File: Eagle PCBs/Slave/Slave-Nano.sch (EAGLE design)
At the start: 15 parts, among them Q1 TIP120

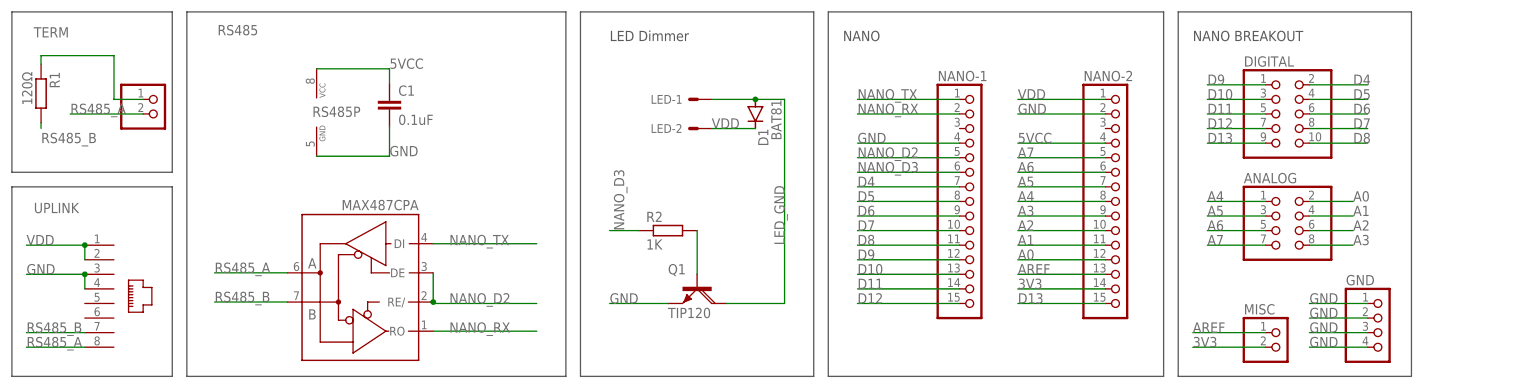
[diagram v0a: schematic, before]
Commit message: Added a 5v bus to all PCBs
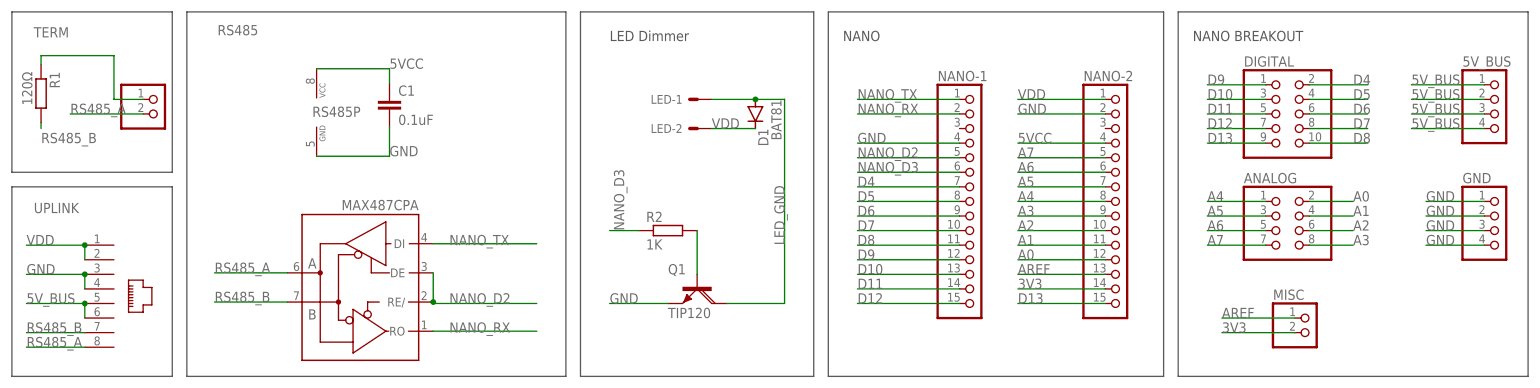
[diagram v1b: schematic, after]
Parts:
- added 5V_BUS: (no value), pinhead:PINHD-1X4
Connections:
- new net 5V_BUS: 5V_BUS.1, 5V_BUS.2, 5V_BUS.3, 5V_BUS.4, UPLINK.5, UPLINK.6
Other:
- moved on the sheet: GND, MISC
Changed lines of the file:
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@@
 <part name="MISC" library="pinhead" library_urn="urn:adsk.eagle:library:325" deviceset="PINHD-1X2" device="" package3d_urn="urn:adsk.eagle:package:22435/2"/>
 <part name="GND" library="pinhead" library_urn="urn:adsk.eagle:library:325" deviceset="PINHD-1X4" device="" package3d_urn="urn:adsk.eagle:package:22407/2"/>
+<part name="5V_BUS" library="pinhead" library_urn="urn:adsk.eagle:library:325" deviceset="PINHD-1X4" device="" package3d_urn="urn:adsk.eagle:package:22407/2"/>
 </parts>
 <sheets>
@@
 <wire x1="144.78" y1="2.54" x2="144.78" y2="66.04" width="0.1524" layer="97"/>
 <text x="147.32" y="60.96" size="1.778" layer="97">NANO</text>
-<wire x1="205.74" y1="66.04" x2="246.38" y2="66.04" width="0.1524" layer="97"/>
-<wire x1="246.38" y1="66.04" x2="246.38" y2="2.54" width="0.1524" layer="97"/>
-<wire x1="246.38" y1="2.54" x2="205.74" y2="2.54" width="0.1524" layer="97"/>
+<wire x1="205.74" y1="66.04" x2="266.7" y2="66.04" width="0.1524" layer="97"/>
+<wire x1="266.7" y1="66.04" x2="266.7" y2="2.54" width="0.1524" layer="97"/>
+<wire x1="266.7" y1="2.54" x2="205.74" y2="2.54" width="0.1524" layer="97"/>
 <wire x1="205.74" y1="2.54" x2="205.74" y2="66.04" width="0.1524" layer="97"/>
 <text x="208.28" y="60.96" size="1.778" layer="97">NANO BREAKOUT</text>
@@
 <attribute name="VALUE" x="217.17" y="20.32" size="1.778" layer="96"/>
 </instance>
-<instance part="MISC" gate="G$1" x="223.52" y="7.62" smashed="yes">
-<attribute name="NAME" x="217.17" y="13.335" size="1.778" layer="95"/>
-<attribute name="VALUE" x="217.17" y="2.54" size="1.778" layer="96"/>
-</instance>
-<instance part="GND" gate="A" x="241.3" y="10.16" smashed="yes">
-<attribute name="NAME" x="234.95" y="18.415" size="1.778" layer="95"/>
-<attribute name="VALUE" x="234.95" y="2.54" size="1.778" layer="96"/>
+<instance part="MISC" gate="G$1" x="228.6" y="10.16" smashed="yes">
+<attribute name="NAME" x="222.25" y="15.875" size="1.778" layer="95"/>
+<attribute name="VALUE" x="222.25" y="5.08" size="1.778" layer="96"/>
+</instance>
+<instance part="GND" gate="A" x="261.62" y="27.94" smashed="yes">
+<attribute name="NAME" x="255.27" y="36.195" size="1.778" layer="95"/>
+<attribute name="VALUE" x="255.27" y="20.32" size="1.778" layer="96"/>
+</instance>
+<instance part="5V_BUS" gate="A" x="261.62" y="48.26" smashed="yes">
+<attribute name="NAME" x="255.27" y="56.515" size="1.778" layer="95"/>
+<attribute name="VALUE" x="255.27" y="40.64" size="1.778" layer="96"/>
 </instance>
 </instances>
@@
 <segment>
 <pinref part="GND" gate="A" pin="1"/>
-<wire x1="238.76" y1="15.24" x2="228.6" y2="15.24" width="0.1524" layer="91"/>
-<label x="228.6" y="15.24" size="1.778" layer="95"/>
-</segment>
-<segment>
-<wire x1="238.76" y1="12.7" x2="228.6" y2="12.7" width="0.1524" layer="91"/>
-<label x="228.6" y="12.7" size="1.778" layer="95"/>
+<wire x1="259.08" y1="33.02" x2="248.92" y2="33.02" width="0.1524" layer="91"/>
+<label x="248.92" y="33.02" size="1.778" layer="95"/>
+</segment>
+<segment>
+<wire x1="259.08" y1="30.48" x2="248.92" y2="30.48" width="0.1524" layer="91"/>
+<label x="248.92" y="30.48" size="1.778" layer="95"/>
 <pinref part="GND" gate="A" pin="2"/>
 </segment>
 <segment>
-<wire x1="238.76" y1="10.16" x2="228.6" y2="10.16" width="0.1524" layer="91"/>
-<label x="228.6" y="10.16" size="1.778" layer="95"/>
+<wire x1="259.08" y1="27.94" x2="248.92" y2="27.94" width="0.1524" layer="91"/>
+<label x="248.92" y="27.94" size="1.778" layer="95"/>
 <pinref part="GND" gate="A" pin="3"/>
 </segment>
 <segment>
-<wire x1="238.76" y1="7.62" x2="228.6" y2="7.62" width="0.1524" layer="91"/>
-<label x="228.6" y="7.62" size="1.778" layer="95"/>
+<wire x1="259.08" y1="25.4" x2="248.92" y2="25.4" width="0.1524" layer="91"/>
+<label x="248.92" y="25.4" size="1.778" layer="95"/>
 <pinref part="GND" gate="A" pin="4"/>
 </segment>
@@
 <segment>
 <pinref part="MISC" gate="G$1" pin="1"/>
-<wire x1="220.98" y1="10.16" x2="208.28" y2="10.16" width="0.1524" layer="91"/>
-<label x="208.28" y="10.16" size="1.778" layer="95"/>
+<wire x1="226.06" y1="12.7" x2="213.36" y2="12.7" width="0.1524" layer="91"/>
+<label x="213.36" y="12.7" size="1.778" layer="95"/>
 </segment>
 </net>
@@
 <segment>
 <pinref part="MISC" gate="G$1" pin="2"/>
-<wire x1="220.98" y1="7.62" x2="208.28" y2="7.62" width="0.1524" layer="91"/>
-<label x="208.28" y="7.62" size="1.778" layer="95"/>
-</segment>
-</net>
+<wire x1="226.06" y1="10.16" x2="213.36" y2="10.16" width="0.1524" layer="91"/>
+<label x="213.36" y="10.16" size="1.778" layer="95"/>
+</segment>
+</net>
+<net name="5V_BUS" class="0">
+<segment>
+<pinref part="UPLINK" gate="G$1" pin="5"/>
+<wire x1="5.08" y1="15.24" x2="15.24" y2="15.24" width="0.1524" layer="91"/>
+<pinref part="UPLINK" gate="G$1" pin="6"/>
+<wire x1="15.24" y1="12.7" x2="15.24" y2="15.24" width="0.1524" layer="91"/>
+<junction x="15.24" y="15.24"/>
+<label x="5.08" y="15.24" size="1.778" layer="95"/>
+</segment>
+<segment>
+<wire x1="246.38" y1="53.34" x2="259.08" y2="53.34" width="0.1524" layer="91"/>
+<label x="246.38" y="53.34" size="1.778" layer="95"/>
+<pinref part="5V_BUS" gate="A" pin="1"/>
+</segment>
+<segment>
+<wire x1="246.38" y1="50.8" x2="259.08" y2="50.8" width="0.1524" layer="91"/>
+<label x="246.38" y="50.8" size="1.778" layer="95"/>
+<pinref part="5V_BUS" gate="A" pin="2"/>
+</segment>
+<segment>
+<wire x1="246.38" y1="48.26" x2="259.08" y2="48.26" width="0.1524" layer="91"/>
+<label x="246.38" y="48.26" size="1.778" layer="95"/>
+<pinref part="5V_BUS" gate="A" pin="3"/>
+</segment>
+<segment>
+<wire x1="246.38" y1="45.72" x2="259.08" y2="45.72" width="0.1524" layer="91"/>
+<label x="246.38" y="45.72" size="1.778" layer="95"/>
+<pinref part="5V_BUS" gate="A" pin="4"/>
+</segment>
+</net>
